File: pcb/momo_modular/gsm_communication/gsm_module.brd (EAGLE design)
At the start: 50.8 x 33 mm, 20 parts, among them U1 PIC16LF1823, U2 TI-HIGHSIDE-PFET, U3 SIM900

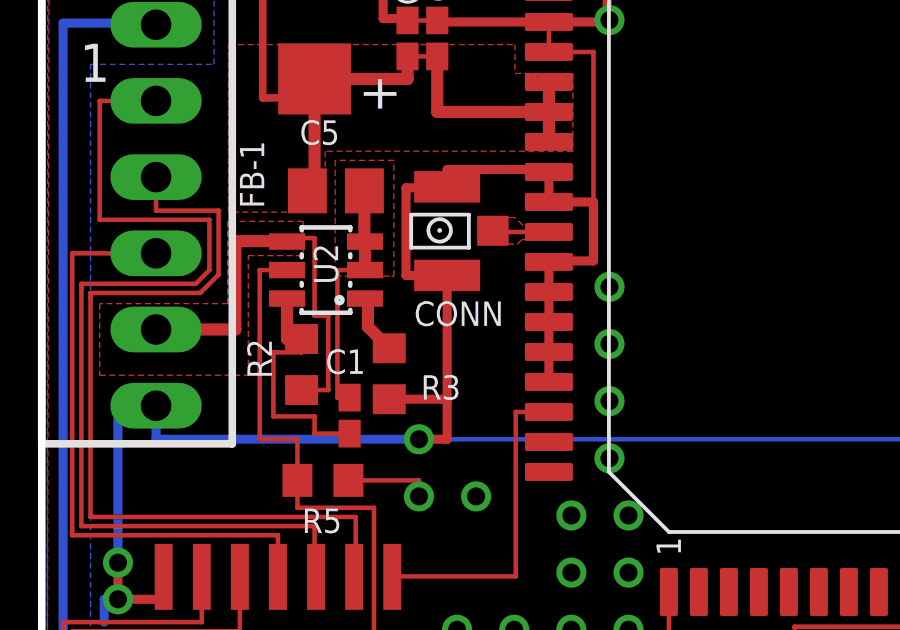
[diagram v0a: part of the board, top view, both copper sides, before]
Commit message: Final review of GSM module
- added all part descriptions and part numbers
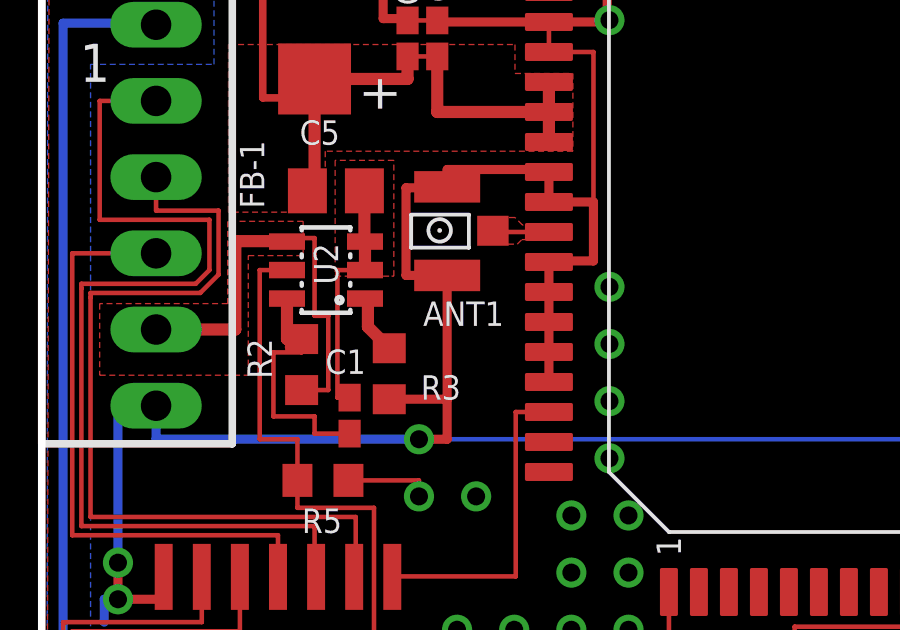
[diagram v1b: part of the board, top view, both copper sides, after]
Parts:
- renumbered CONN to ANT1
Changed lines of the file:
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@@
 <attribute name="PARTNAME" value="gsm_module"/>
 <attribute name="REVISION" value="3.0"/>
-<attribute name="WIDTH" value="2.7"/>
+<attribute name="WIDTH" value="2.0"/>
 </attributes>
 <variantdefs>
@@
 <attribute name="NAME" x="11.684" y="27.6352" size="0.8128" layer="25" rot="R270"/>
 <attribute name="DIGIKEY-PN" value="445-1567-1-ND" x="14.8844" y="25.9588" size="1.778" layer="27" rot="R180" display="off"/>
-</element>
-<element name="CONN" library="components" package="RFJACK" value="RFANTENNA" x="17.3228" y="23.1394" smashed="yes">
+<attribute name="DESCRIPTION" value="Ferrite Bead" x="14.8844" y="25.9588" size="1.778" layer="27" rot="R180" display="off"/>
+<attribute name="FOOTPRINT" value="SMD 0805" x="14.8844" y="25.9588" size="1.778" layer="27" rot="R180" display="off"/>
+</element>
+<element name="ANT1" library="components" package="RFJACK" value="RFANTENNA" x="17.3228" y="23.1394" smashed="yes">
 <attribute name="NAME" x="20.4798" y="22.2688" size="0.8128" layer="25" rot="R180"/>
 <attribute name="DIGIKEY-PN" value="J983CT-ND" x="17.3228" y="23.1394" size="1.778" layer="27" display="off"/>
+<attribute name="DESCRIPTION" value="RF antenna connector u.fl " x="17.3228" y="23.1394" size="1.778" layer="27" display="off"/>
+<attribute name="FOOTPRINT" value="Custom SMD" x="17.3228" y="23.1394" size="1.778" layer="27" display="off"/>
 </element>
 <element name="C3" library="rcl" package="C0402" value="100 nF" x="6.858" y="7.3406" smashed="yes" rot="R270">
@@
 <attribute name="NAME" x="44.8056" y="6.2484" size="0.8128" layer="25" ratio="10" rot="R180"/>
 <attribute name="VALUE" x="47.6758" y="11.43" size="1.27" layer="27" rot="R180"/>
-<attribute name="DIGIKEY-PN" value="A19430-ND" x="43.8658" y="8.255" size="1.778" layer="27" rot="R180" display="off"/>
+<attribute name="POPULATE" value="no" x="43.8658" y="8.255" size="1.778" layer="27" rot="R180" display="off"/>
 </element>
 <element name="R5" library="rcl" package="R0603" value="100K" x="14.4526" y="16.3068" smashed="yes" rot="R180">
@@
 <element name="JP1" library="components" package="MOMO-EDGE-6M" value="MOMO-EDGE-6M" x="8.89" y="21.336">
 <attribute name="DIGIKEY-PN" value="609-3327-ND" x="8.89" y="21.336" size="1.778" layer="27" display="off"/>
+<attribute name="DESCRIPTION" value="6 pin r/a male header" x="8.89" y="21.336" size="1.778" layer="27" display="off"/>
+<attribute name="FOOTPRINT" value="Through Hole" x="8.89" y="21.336" size="1.778" layer="27" display="off"/>
 </element>
 <element name="U1" library="components" package="SO14" value="PIC16LF1823" x="12.954" y="10.4902" smashed="yes">
 <attribute name="NAME" x="13.97" y="11.1252" size="0.8128" layer="25" rot="R180"/>
 <attribute name="DIGIKEY-PN" value="PIC16LF1823-I/SL-ND" x="12.954" y="10.4902" size="1.778" layer="27" display="off"/>
+<attribute name="DESCRIPTION" value="PIC 16lf1823 microcontroller" x="12.954" y="10.4902" size="1.778" layer="27" display="off"/>
 </element>
 <element name="U2" library="components" package="SOT23-6L" value="TI-HIGHSIDE-PFET" x="14.5542" y="23.3172" smashed="yes" rot="R90">
 <attribute name="DIGIKEY-PN" value="296-34970-1-ND" x="14.5542" y="23.3172" size="1.778" layer="27" rot="R90" display="off"/>
 <attribute name="NAME" x="14.9606" y="22.8346" size="0.8128" layer="25" rot="R90"/>
+<attribute name="DESCRIPTION" value="TPS27081 Highside Load Controller" x="14.5542" y="23.3172" size="1.778" layer="27" rot="R90" display="off"/>
 </element>
 <element name="U3" library="components" package="SIM900" value="SIM900" x="33.9852" y="24.5872" rot="R90">
 <attribute name="MANU" value="SIMCOM" x="33.9852" y="24.5872" size="1.778" layer="27" rot="R90" display="off"/>
 <attribute name="MPN" value="SIM900" x="33.9852" y="24.5872" size="1.778" layer="27" rot="R90" display="off"/>
+<attribute name="DESCRIPTION" value="SIM900 GSM/GPRS Quadband GSM Modem" x="33.9852" y="24.5872" size="1.778" layer="27" rot="R90" display="off"/>
+<attribute name="FOOTPRINT" value="Custom SMD" x="33.9852" y="24.5872" size="1.778" layer="27" rot="R90" display="off"/>
 </element>
 <element name="C5" library="components" package="2917" value="330 uF" x="14.1732" y="31.623" smashed="yes" rot="R270">
@@
 <attribute name="VALUE" x="6.985" y="34.3408" size="1.27" layer="27"/>
 <attribute name="DIGIKEY-PN" value="475-2709-1-ND" x="8.255" y="36.2458" size="0.8128" layer="27" rot="R270" display="off"/>
+<attribute name="DESCRIPTION" value="Green Chip LED" x="8.255" y="36.2458" size="1.778" layer="27" rot="R270" display="off"/>
+<attribute name="FOOTPRINT" value="SMD 0603" x="8.255" y="36.2458" size="1.778" layer="27" rot="R270" display="off"/>
 </element>
 <element name="R6" library="rcl" package="R0603" value="470R" x="18.7706" y="36.2712" smashed="yes" rot="R180">
@@
 <attribute name="NAME" x="49.6824" y="28.5242" size="1.27" layer="25" ratio="10" rot="R90"/>
 <attribute name="VALUE" x="48.9458" y="31.75" size="1.27" layer="27" rot="R270"/>
+<attribute name="DIGIKEY-PN" value="S1012EC-07-ND" x="52.1208" y="22.86" size="1.778" layer="27" rot="R270" display="off"/>
+<attribute name="DESCRIPTION" value="7 pin vertical male header" x="52.1208" y="22.86" size="1.778" layer="27" rot="R270" display="off"/>
+<attribute name="FOOTPRINT" value="Through Hole" x="52.1208" y="22.86" size="1.778" layer="27" rot="R270" display="off"/>
 </element>
 </elements>
@@
 <signal name="GND">
 <contactref element="R3" pad="1"/>
-<contactref element="CONN" pad="UNUSED1"/>
-<contactref element="CONN" pad="UNUSED2"/>
+<contactref element="ANT1" pad="UNUSED1"/>
+<contactref element="ANT1" pad="UNUSED2"/>
 <contactref element="C3" pad="2"/>
 <contactref element="JP2" pad="3"/>
@@
 </signal>
 <signal name="N$7">
-<contactref element="CONN" pad="ANTENNA"/>
+<contactref element="ANT1" pad="ANTENNA"/>
 <contactref element="U3" pad="60"/>
 <wire x1="20.1178" y1="24.6269" x2="20.1178" y2="24.5872" width="0.1524" layer="1"/>
